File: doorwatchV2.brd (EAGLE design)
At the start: 91.4 x 77.5 mm, 44 parts, among them IC1 LM2576S-5.0, IC2 MAX3232CPE, K1 FINDER-43.61, Q1 IRLZ44Z, T1 BC847, T2 BC847, T3 BC847, T4 BC847, X1 MKDSN1,5/2-5,08, X2 D-SUB9-H2M09RA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

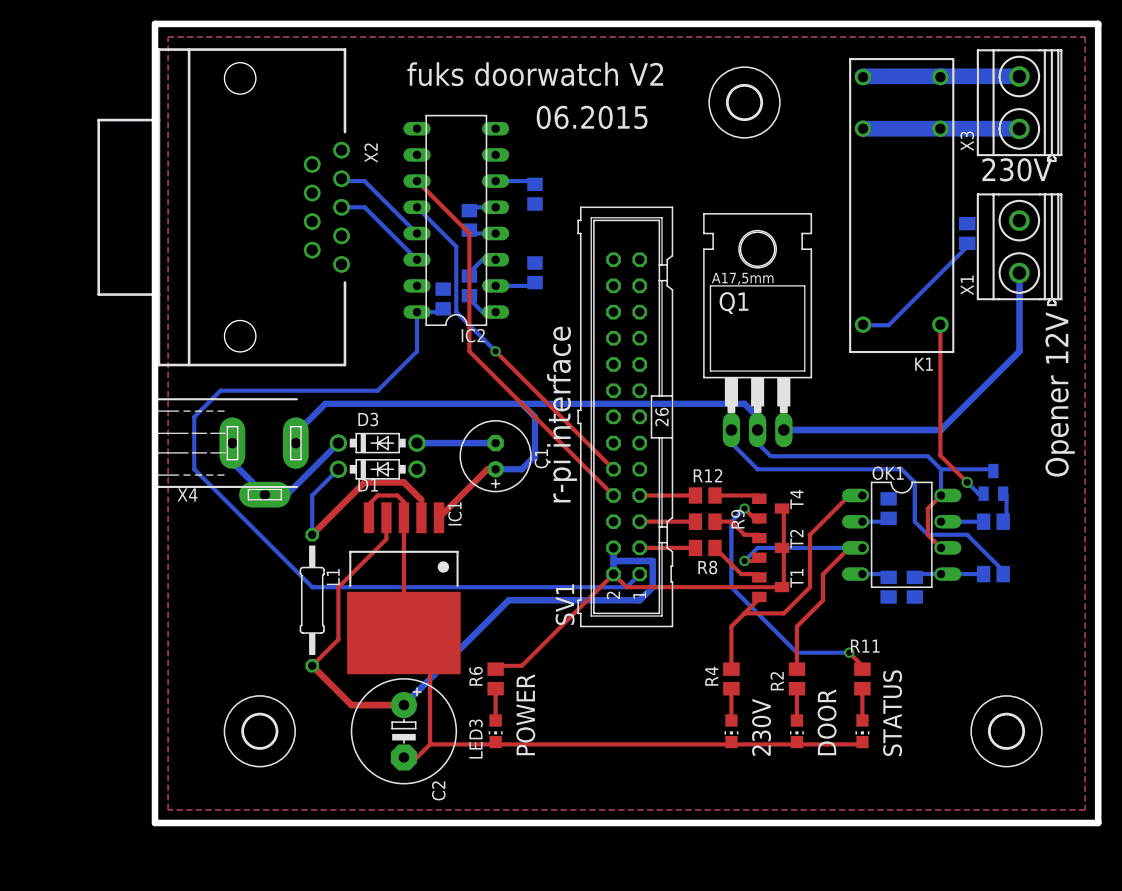
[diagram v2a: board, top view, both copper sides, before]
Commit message: updated the package of the inductor and updated the layout
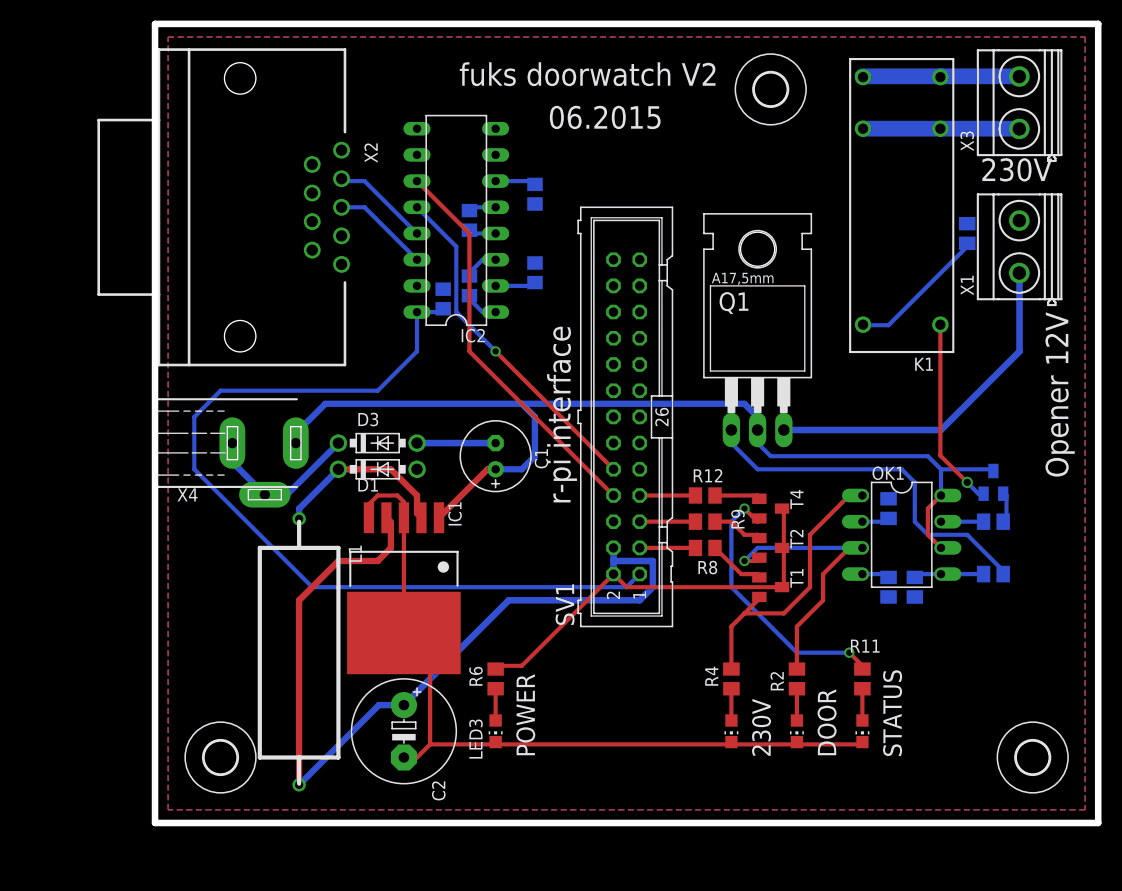
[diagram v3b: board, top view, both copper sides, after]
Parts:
- L1: device rcl:0207/12 -> rcl:2200-20.32
- moved H1 4.58 mm to (5.08, 30.5)
- moved H3 3.59 mm to (83.8, 30.5)
- moved H2 2.84 mm to (58.4, 95.2)
- moved L1 1.27 mm to (12.7, 45.7)
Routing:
- net +5V: track 106.0 -> 123.5 mm
- net N$3: track 22.5 -> 17.4 mm
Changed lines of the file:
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@@
 <dimension x1="-1.27" y1="101.6" x2="90.17" y2="101.6" x3="44.45" y3="105.41" layer="48"/>
 <dimension x1="-1.27" y1="24.13" x2="-1.27" y2="101.6" x3="-10.16" y3="62.865" layer="48"/>
-<text x="48.26" y="97.79" size="2.1844" layer="25" rot="R180">fuks doorwatch V2</text>
+<text x="53.34" y="97.79" size="2.1844" layer="25" rot="R180">fuks doorwatch V2</text>
 <text x="36.83" y="72.39" size="2.1844" layer="25" rot="R270">r-pi interface</text>
-<text x="35.56" y="91.44" size="2.1844" layer="25">06.2015</text>
+<text x="36.83" y="91.44" size="2.1844" layer="25">06.2015</text>
 <text x="85.09" y="73.66" size="2.1844" layer="21" rot="R270">Opener 12V</text>
 <text x="78.74" y="86.36" size="2.1844" layer="21">230V</text>
@@
 <elements>
 <element name="IC1" library="regulators" package="TO263-5" value="LM2576S-5.0" x="22.86" y="45.72" rot="R180"/>
-<element name="L1" library="rcl" package="0207/12" value="100uH" x="13.97" y="45.72" rot="R270"/>
+<element name="L1" library="rcl" package="2200-20.32" value="100uH" x="12.7" y="45.72" rot="R270"/>
 <element name="D1" library="diode" package="DO41-7.6" value="1N5817-B" x="20.32" y="58.42" smashed="yes">
 <attribute name="NAME" x="18.288" y="56.261" size="1.27" layer="25" ratio="10"/>
@@
 <element name="T4" library="transistor" package="SOT23" value="BC847" x="58.42" y="54.61" rot="R270"/>
 <element name="R12" library="rcl" package="M0805" value="1k" x="52.07" y="55.88"/>
-<element name="H1" library="holes" package="3,2" value="MOUNT-HOLE3.2" x="8.89" y="33.02"/>
-<element name="H2" library="holes" package="3,2" value="MOUNT-HOLE3.2" x="55.88" y="93.98"/>
-<element name="H3" library="holes" package="3,2" value="MOUNT-HOLE3.2" x="81.28" y="33.02"/>
+<element name="H1" library="holes" package="3,2" value="MOUNT-HOLE3.2" x="5.08" y="30.48"/>
+<element name="H2" library="holes" package="3,2" value="MOUNT-HOLE3.2" x="58.42" y="95.25"/>
+<element name="H3" library="holes" package="3,2" value="MOUNT-HOLE3.2" x="83.82" y="30.48"/>
 <element name="R13" library="rcl" package="M0805" value="1k" x="72.39" y="46.99" rot="MR90"/>
 </elements>
@@
 <contactref element="D1" pad="C"/>
 <contactref element="L1" pad="1"/>
-<wire x1="24.56" y1="53.72" x2="24.56" y2="55.45" width="0.4064" layer="1"/>
-<wire x1="24.56" y1="55.45" x2="22.86" y2="57.15" width="0.635" layer="1"/>
-<wire x1="22.86" y1="57.15" x2="19.05" y2="57.15" width="0.635" layer="1"/>
-<wire x1="13.97" y1="55.88" x2="13.97" y2="52.07" width="0.4064" layer="16"/>
-<wire x1="19.05" y1="57.15" x2="13.97" y2="52.07" width="0.635" layer="1"/>
-<wire x1="16.51" y1="58.42" x2="13.97" y2="55.88" width="0.4064" layer="16"/>
+<wire x1="16.51" y1="58.42" x2="12.7" y2="54.61" width="0.6096" layer="16"/>
+<wire x1="12.7" y1="54.61" x2="12.7" y2="53.61" width="0.6096" layer="16"/>
+<wire x1="24.56" y1="53.72" x2="24.13" y2="54.15" width="0.6096" layer="1"/>
+<wire x1="24.13" y1="54.15" x2="24.13" y2="55.88" width="0.6096" layer="1"/>
+<wire x1="24.13" y1="55.88" x2="21.59" y2="58.42" width="0.6096" layer="1"/>
+<wire x1="21.59" y1="58.42" x2="16.51" y2="58.42" width="0.6096" layer="1"/>
 </signal>
 <signal name="+5V">
@@
 <wire x1="34.29" y1="39.37" x2="43.18" y2="48.26" width="0.4064" layer="1"/>
 <contactref element="L1" pad="2"/>
-<wire x1="21.16" y1="53.72" x2="21.16" y2="51.64" width="0.4064" layer="1"/>
-<wire x1="17.78" y1="35.56" x2="22.86" y2="35.56" width="0.635" layer="1"/>
-<wire x1="13.97" y1="39.37" x2="17.78" y2="35.56" width="0.635" layer="1"/>
-<wire x1="21.16" y1="51.64" x2="16.51" y2="46.99" width="0.4064" layer="1"/>
-<wire x1="16.51" y1="46.99" x2="16.51" y2="41.91" width="0.4064" layer="1"/>
-<wire x1="16.51" y1="41.91" x2="13.97" y2="39.37" width="0.4064" layer="1"/>
+<wire x1="12.7" y1="27.83" x2="20.43" y2="35.56" width="0.6096" layer="16"/>
+<wire x1="20.43" y1="35.56" x2="22.86" y2="35.56" width="0.6096" layer="16"/>
+<wire x1="21.16" y1="53.72" x2="21.59" y2="53.29" width="0.6096" layer="1"/>
+<wire x1="21.59" y1="53.29" x2="21.59" y2="50.8" width="0.6096" layer="1"/>
+<wire x1="21.59" y1="50.8" x2="20.32" y2="49.53" width="0.6096" layer="1"/>
+<wire x1="20.32" y1="49.53" x2="16.51" y2="49.53" width="0.6096" layer="1"/>
+<wire x1="16.51" y1="49.53" x2="12.7" y2="45.72" width="0.6096" layer="1"/>
+<wire x1="12.7" y1="45.72" x2="12.7" y2="27.83" width="0.6096" layer="1"/>
 </signal>
 <signal name="+3V3">

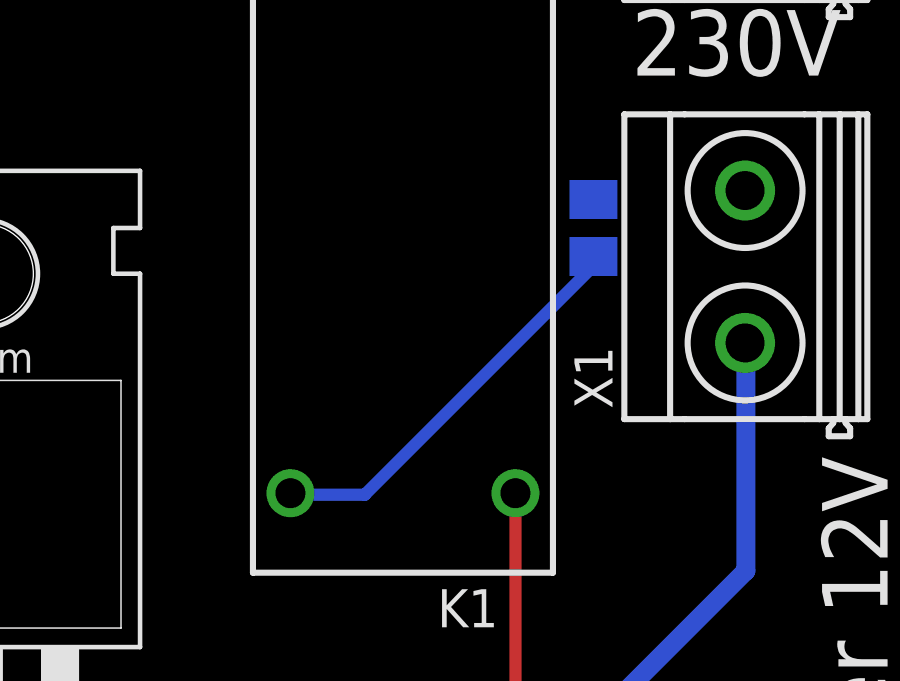
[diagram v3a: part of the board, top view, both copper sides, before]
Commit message: removed resistor in relai circuit -> voltage was to low
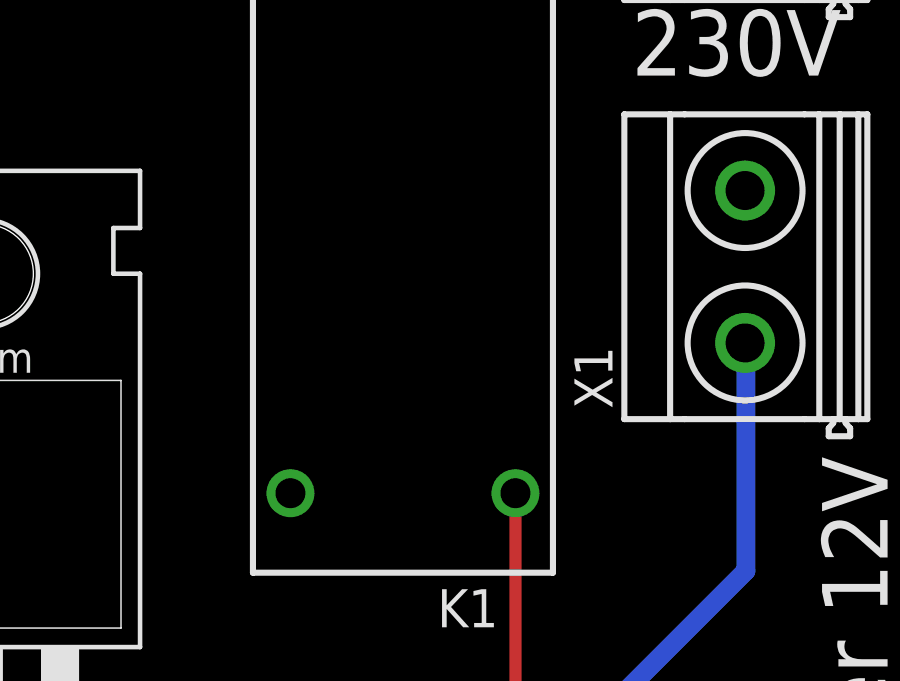
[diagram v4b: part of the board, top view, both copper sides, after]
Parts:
- removed R10: 330, rcl:M0805
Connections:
- removed net N$26: K1.A2, R10.2
- net GND: now also K1.A2; no longer R10.1
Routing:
- net N$26: track 13.7 -> 0.00 mm
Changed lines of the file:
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@@
 </element>
 <element name="T3" library="transistor" package="SOT23" value="BC847" x="80.01" y="57.15" rot="MR0"/>
-<element name="R10" library="rcl" package="M0805" value="330" x="77.47" y="81.28" rot="MR270"/>
 <element name="LED4" library="led" package="CHIP-LED0805" value="" x="67.31" y="33.02" smashed="yes" rot="R180">
 <attribute name="VALUE" x="64.77" y="34.29" size="1.27" layer="27" rot="R270"/>
@@
 <contactref element="R1" pad="2"/>
 <contactref element="LED1" pad="C"/>
-<contactref element="R10" pad="1"/>
 <contactref element="R5" pad="1"/>
 <contactref element="LED2" pad="C"/>
@@
 <wire x1="22.225" y1="55.88" x2="22.86" y2="55.245" width="0.4064" layer="1"/>
 <contactref element="R13" pad="1"/>
+<contactref element="K1" pad="A2"/>
 </signal>
 <signal name="N$3">
@@
 <wire x1="78.57" y1="56.05" x2="79.06" y2="56.05" width="0.4064" layer="16"/>
 </signal>
-<signal name="N$26">
-<contactref element="K1" pad="A2"/>
-<contactref element="R10" pad="2"/>
-<wire x1="69.85" y1="72.39" x2="77.47" y2="80.01" width="0.4064" layer="16"/>
-<wire x1="67.31" y1="72.39" x2="69.85" y2="72.39" width="0.4064" layer="16"/>
-<wire x1="77.47" y1="80.01" x2="77.47" y2="80.33" width="0.4064" layer="16"/>
-<wire x1="67.31" y1="72.39" x2="67.37" y2="72.44" width="0.4064" layer="16"/>
-</signal>
 <signal name="N$27">
